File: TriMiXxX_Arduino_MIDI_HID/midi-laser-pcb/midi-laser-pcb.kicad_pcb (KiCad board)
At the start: 2 copper layers, 100 x 75 mm, 32 parts, among them J1 Jogwheel, J2 UART_PI, J3 PLAY_CUE, J4 TRACK_ENCODER, J5 LOOP_SIZE, J6 LOOP, J7 TEMPO, J8 I2C, SW1 Arduino_RST, U1 ProMicro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

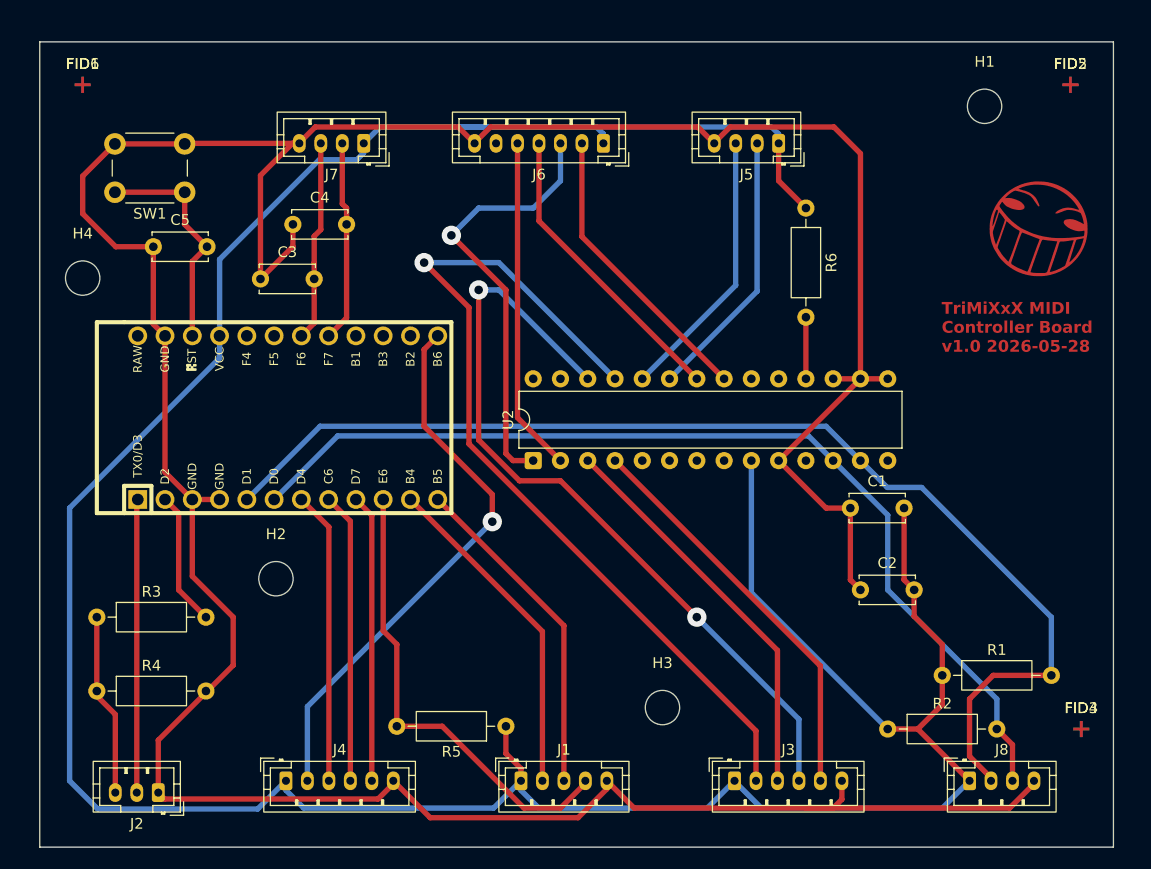
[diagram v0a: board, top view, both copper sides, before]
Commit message: Update schematics for jlcpcb productions, new dims, and sunlu petgcf calibration
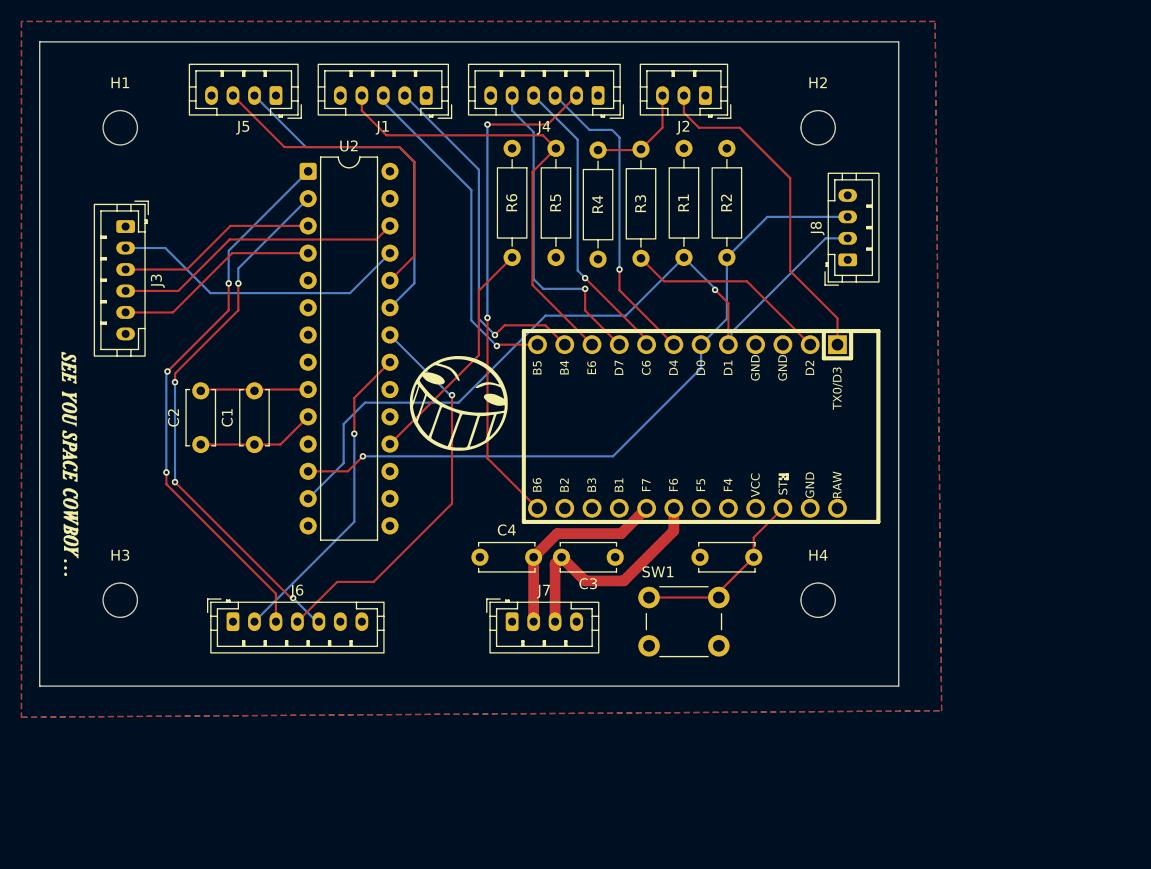
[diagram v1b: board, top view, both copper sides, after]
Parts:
- removed FID1, FID2, FID3, FID4, FID5, FID6: Fiducial, Fiducial:Fiducial_Cross_1.5mm_Mask2mm
- moved J2 82.5 mm to (77.0, 20.0)
- moved H1 80.5 mm to (22.5, 23.0)
- moved J3 76.7 mm to (23.0, 32.2), turned to -90 degrees
- moved H4 74.8 mm to (87.5, 67.0)
- moved J4 70.1 mm to (67.0, 20.0), turned to 180 degrees
- moved R4 68.7 mm to (67.0, 25.1), turned to -90 degrees
- moved R3 66.8 mm to (71.0, 25.0), turned to -90 degrees
- moved H2 65.7 mm to (87.5, 23.0)
- moved J1 64.4 mm to (51.0, 20.0), turned to 180 degrees
- moved C2 62.9 mm to (30.0, 52.5), turned to 90 degrees
- moved C5 58.6 mm to (76.5, 63.0)
- moved SW1 57.4 mm to (71.8, 66.8), turned to 0 degrees
- moved J6 56.3 mm to (33.0, 69.0), turned to 0 degrees
- moved R2 56.1 mm to (79.0, 24.9), turned to -90 degrees
- moved C1 55.8 mm to (35.0, 52.5), turned to 90 degrees
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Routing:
- net GND: track 316.8 -> 11.1 mm
- net +5V: track 304.6 -> 10.0 mm
- net /BTN_PLAY: track 83.3 -> 27.9 mm, vias 1 -> 0
- net /BTN_CUE: track 73.9 -> 27.1 mm, vias 2 -> 0
- net /I2C_SDA: track 107.5 -> 71.9 mm, vias 0 -> 1
- net /I2C_SCL: track 92.2 -> 64.7 mm, vias 0 -> 1
- net /LOOP_END_LED: track 31.2 -> 50.3 mm, vias 0 -> 4
- net /LED_CUE: track 37.7 -> 19.3 mm
- net /LED_PLAY: track 37.1 -> 18.7 mm
- net Net-(U2-~{RESET}): track 5.74 -> 22.1 mm
- net /LOOP_START_LED: track 41.0 -> 51.6 mm, vias 1 -> 3
- net /LOOP_END_BTN: track 28.0 -> 37.2 mm, vias 0 -> 1
- net /UART_RX_FROM_PI: track 17.0 -> 9.86 mm
- net /LOOP_HLF_BTN: track 25.3 -> 32.0 mm
- net Net-(U1-RX1/PD2): track 12.5 -> 19.1 mm
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- added copper zone on F.Cu, net +5V
- added copper zone on B.Cu, net GND
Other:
- board size 100 x 75 mm -> 80 x 60 mm
- board text added: "TriMiXxX MIDI Control Board V1"
- board text removed: "TriMiXxX MIDI Controller Board v1.0 2026-05-28"

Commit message: Add some stuff
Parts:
- moved J6 0.10 mm to (33.1, 69.0)
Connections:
- R3 pad 1: /UART_RX_FROM_PI -> /UART_TX_TO_PI
- R3 pad 2: Net-(U1-RX1/PD2) -> Net-(U1-TX0/PD3)
- R4 pad 1: /UART_RX_FROM_PI -> /UART_TX_TO_PI
- U1 pad 1: /UART_TX_TO_PI -> Net-(U1-TX0/PD3)
- U1 pad 2: Net-(U1-RX1/PD2) -> /UART_RX_FROM_PI
- U2 pad 27: unconnected-(U2-GPA6-Pad27) -> /RELOOP_BTN
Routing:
- net /RELOOP_BTN: track 0.00 -> 63.8 mm, vias 0 -> 5
- net /UART_RX_FROM_PI: track 9.86 -> 53.1 mm
- net Net-(U1-TX0/PD3): track 0.00 -> 21.6 mm
- net /UART_TX_TO_PI: track 31.3 -> 11.5 mm
- net Net-(U1-RX1/PD2): track 19.1 -> 0.00 mm
- net /LOOP_END_LED: track 50.3 -> 55.4 mm
- net /LOOP_START_LED: track 51.6 -> 54.9 mm
- net /LOOP_START_BTN: track 29.4 -> 31.7 mm
- net /ENC_SW: track 29.6 -> 28.4 mm
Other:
- board text added: "TriMiXxX MIDI Control Board V2"
- board text removed: "TriMiXxX MIDI Control Board V1"
